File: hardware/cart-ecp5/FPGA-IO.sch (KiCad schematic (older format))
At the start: 9 parts, among them J1 JTAG, U1 LFE5U-25F-xBG256x, U2 W25Q128JVSIM, X1 XO_Generic_NC

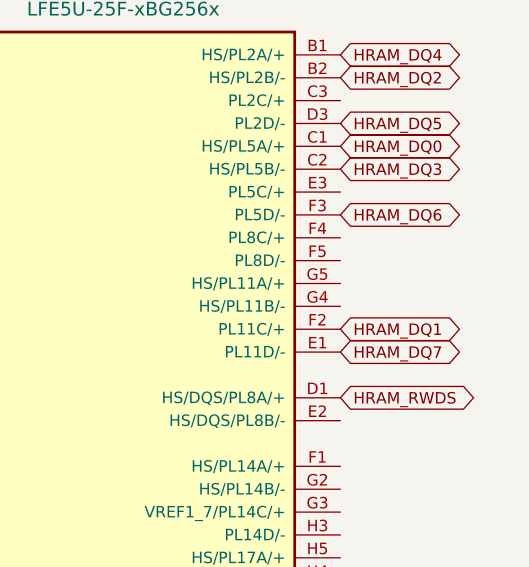
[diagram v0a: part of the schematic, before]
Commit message: First attempt at length tuning hyperram interface
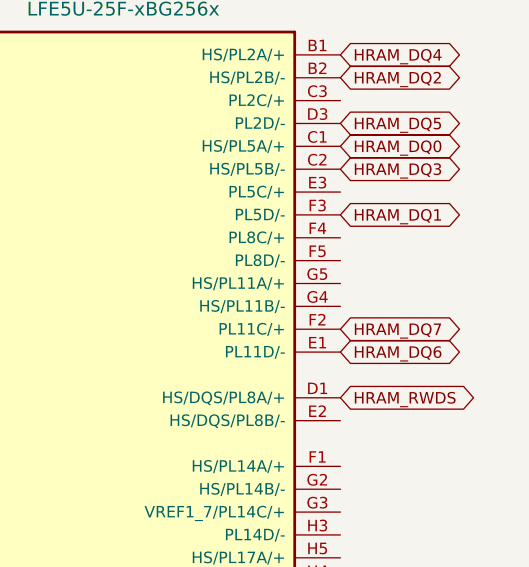
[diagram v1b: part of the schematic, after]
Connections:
- net HRAM_DQ1: now also U1.F3 (PL5D/-); no longer U1.F2 (PL11C/+)
- net HRAM_DQ6: now also U1.E1 (PL11D/-); no longer U1.F3 (PL5D/-)
- net HRAM_DQ7: now also U1.F2 (PL11C/+); no longer U1.E1 (PL11D/-)
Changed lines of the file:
@@
 Text GLabel 13700 6000 2    50   BiDi ~ 0
 HRAM_DQ0
-Text GLabel 13700 6800 2    50   BiDi ~ 0
+Text GLabel 13700 6300 2    50   BiDi ~ 0
 HRAM_DQ1
 Text GLabel 13700 5700 2    50   BiDi ~ 0
@@
 Text GLabel 13700 5900 2    50   BiDi ~ 0
 HRAM_DQ5
-Text GLabel 13700 6300 2    50   BiDi ~ 0
+Text GLabel 13700 6900 2    50   BiDi ~ 0
 HRAM_DQ6
-Text GLabel 13700 6900 2    50   BiDi ~ 0
+Text GLabel 13700 6800 2    50   BiDi ~ 0
 HRAM_DQ7
 Text GLabel 13700 7100 2    50   BiDi ~ 0

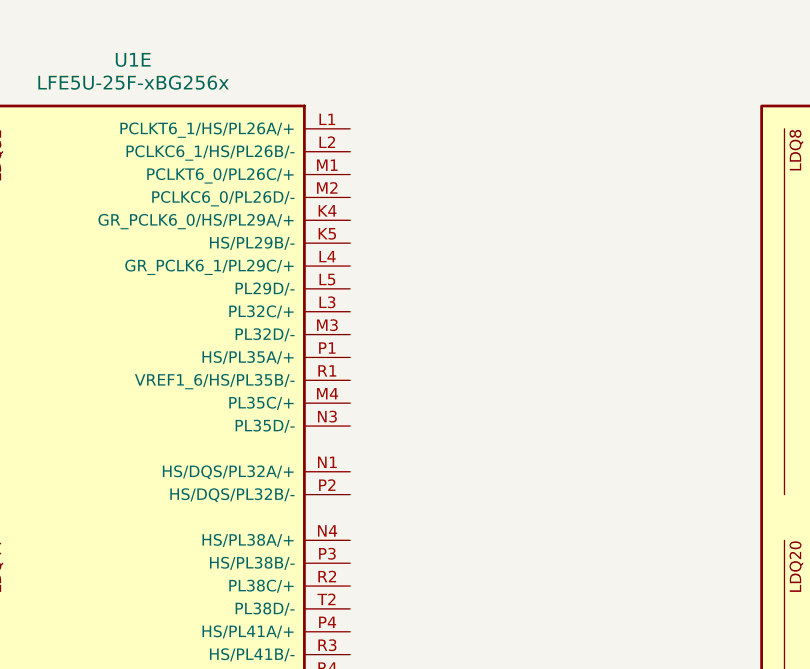
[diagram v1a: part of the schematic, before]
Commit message: Preliminary pin assignment for MicroSD interface
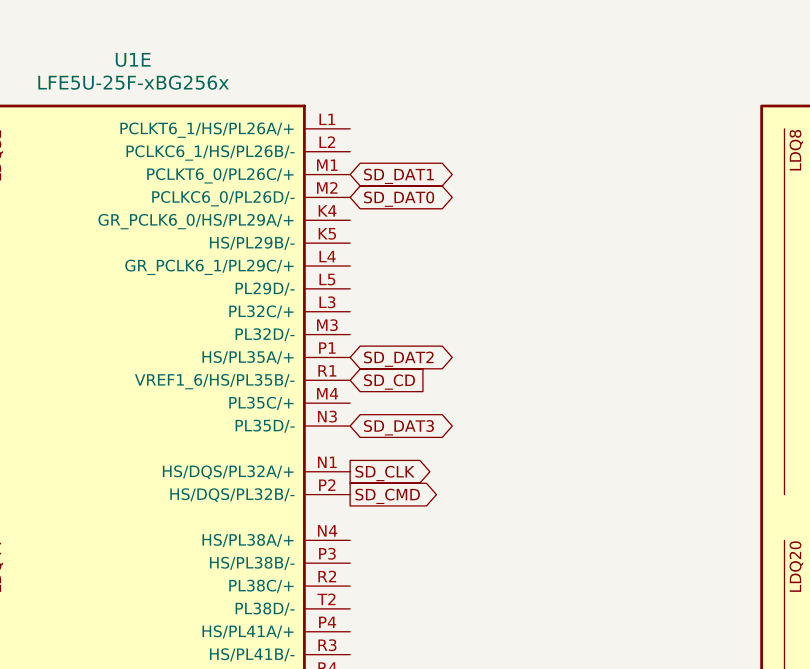
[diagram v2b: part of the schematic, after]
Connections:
- net SD_DAT1: now reaches U1.M1 (PCLKT6_0/PL26C/+)
- net SD_DAT0: now reaches U1.M2 (PCLKC6_0/PL26D/-)
- net SD_CLK: now reaches U1.N1 (HS/DQS/PL32A/+)
- net SD_DAT3: now reaches U1.N3 (PL35D/-)
- net SD_DAT2: now reaches U1.P1 (HS/PL35A/+)
- net SD_CMD: now reaches U1.P2 (HS/DQS/PL32B/-)
- net SD_CD: now reaches U1.R1 (VREF1_6/HS/PL35B/-)
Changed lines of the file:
@@
 Text GLabel 13700 8700 2    50   Output ~ 0
 HRAM_RESET_B
+Text GLabel 10200 7100 2    50   Output ~ 0
+SD_CLK
+Text GLabel 10200 5900 2    50   BiDi ~ 0
+SD_DAT0
+Text GLabel 10200 5800 2    50   BiDi ~ 0
+SD_DAT1
+Text GLabel 10200 7200 2    50   Output ~ 0
+SD_CMD
+Text GLabel 10200 6900 2    50   BiDi ~ 0
+SD_DAT3
+Text GLabel 10200 6600 2    50   BiDi ~ 0
+SD_DAT2
+Text GLabel 10200 6700 2    50   Input ~ 0
+SD_CD
 $EndSCHEMATC

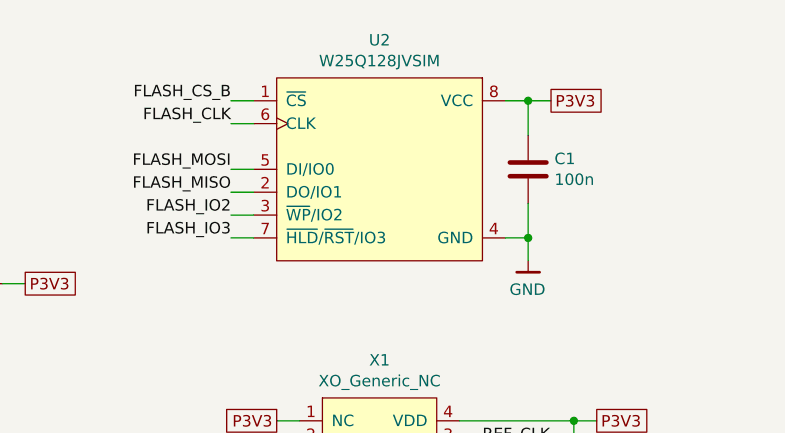
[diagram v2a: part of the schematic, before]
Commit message: Update config flash to WSON package, add HyperRAM decoupling
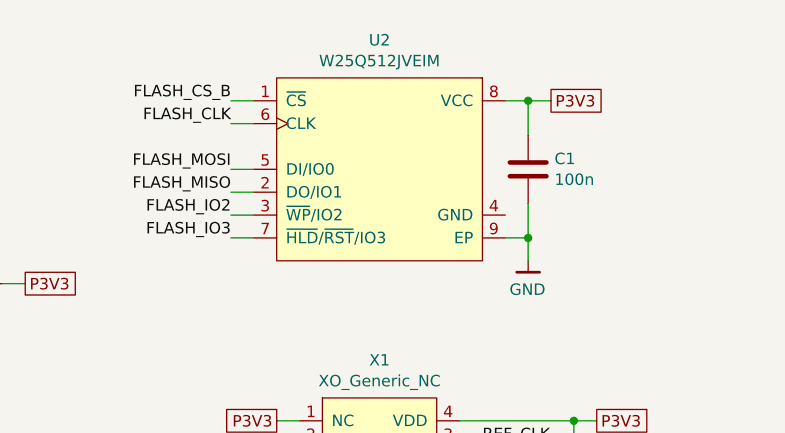
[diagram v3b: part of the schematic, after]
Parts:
- removed U2: W25Q128JVSIM, Package_SO:SOIC-8_5.275x5.275mm_P1.27mm, symbol ng_memory:W25Q128JVSIM
- added U2: W25Q512JVEIM, Package_SON:WSON-8-1EP_6x5mm_P1.27mm_EP3.4x4.3mm, symbol ng_memory:W25Q512JVEIM
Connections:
- net FLASH_CLK: now also U2.6 (CLK)
- net FLASH_CS_B: now also U2.1 (~CS)
- net FLASH_IO2: now also U2.3 (~WP~/IO2)
- net FLASH_IO3: now also U2.7 (~HLD~/~RST~/IO3)
- net FLASH_MISO: now also U2.2 (DO/IO1)
- net FLASH_MOSI: now also U2.5 (DI/IO0)
- net GND: now also U2.9 (EP)
- net P3V3: now also U2.8 (VCC)
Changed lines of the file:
@@
 Comment4 ""
 $EndDescr
-$Comp
-L ng_memory:W25Q128JVSIM U2
-U 1 1 5F3FC315
-P 13200 1500
-F 0 "U2" H 13650 1665 50  0000 C CNN
-F 1 "W25Q128JVSIM" H 13650 1574 50  0000 C CNN
-F 2 "Package_SO:SOIC-8_5.275x5.275mm_P1.27mm" H 13700 650 50  0001 C CNN
-F 3 "https://www.mouser.com/datasheet/2/949/w25q32jv_dtr_revg_03272018_plus-1489786.pdf" H 14200 1200 50  0001 C CNN
-	1    13200 1500
-	-1   0    0    -1
-$EndComp
 Wire Wire Line
 	12200 1600 12100 1600
@@
 Text GLabel 10200 6700 2    50   Input ~ 0
 SD_CD
+$Comp
+L ng_memory:W25Q512JVEIM U2
+U 1 1 5F5A1820
+P 13200 1500
+F 0 "U2" H 13650 1665 50  0000 C CNN
+F 1 "W25Q512JVEIM" H 13650 1574 50  0000 C CNN
+F 2 "Package_SON:WSON-8-1EP_6x5mm_P1.27mm_EP3.4x4.3mm" H 13650 650 50  0001 C CNN
+F 3 "https://www.winbond.com/resource-files/W25Q512JV%20DTR%20RevC%2009102019%20133.pdf" H 14200 1200 50  0001 C CNN
+	1    13200 1500
+	-1   0    0    -1
+$EndComp
 $EndSCHEMATC

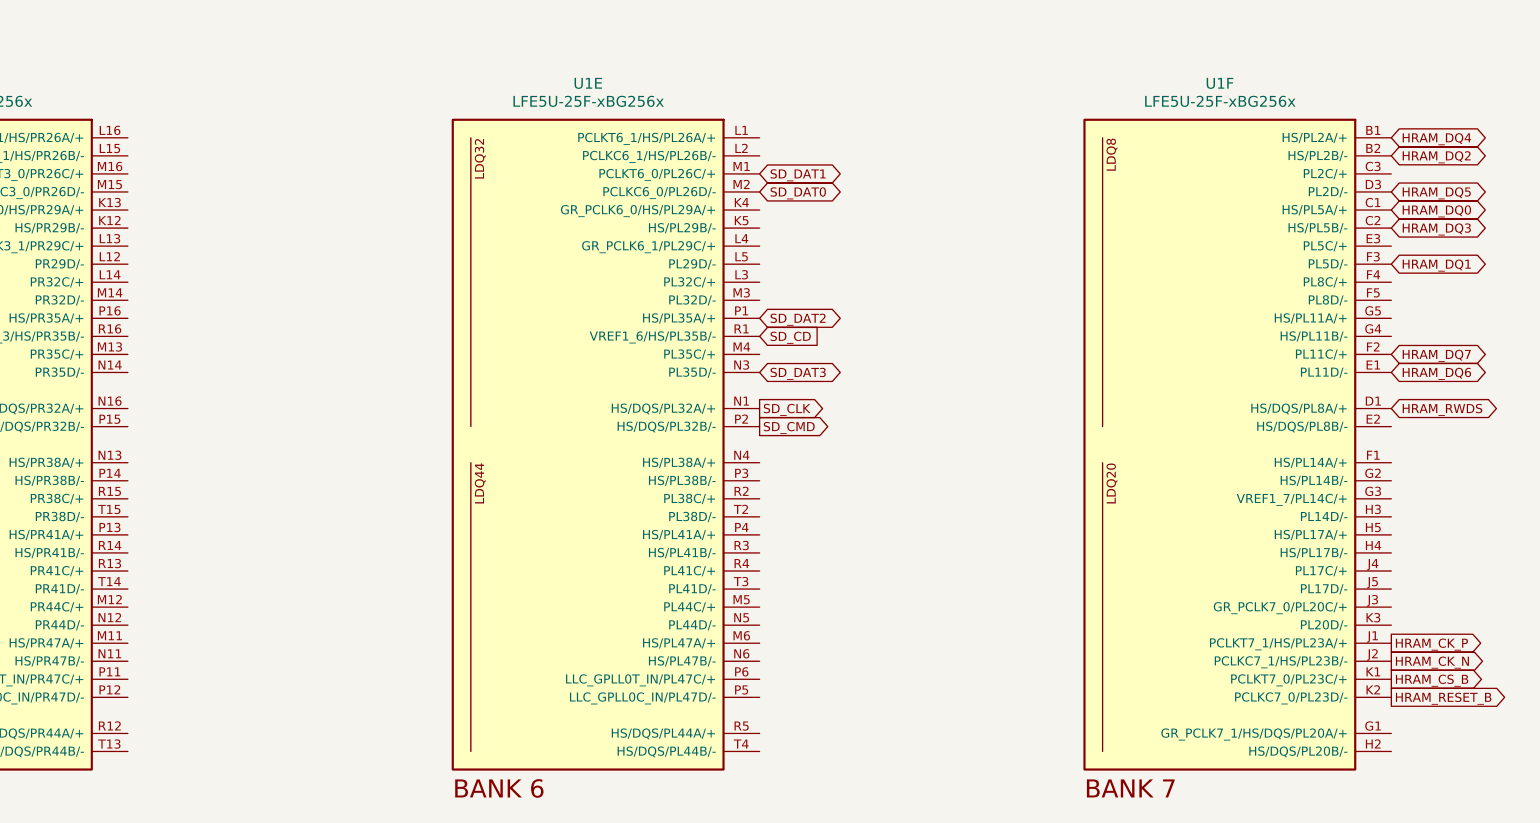
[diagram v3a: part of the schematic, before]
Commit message: Assign FPGA pins to USB interface
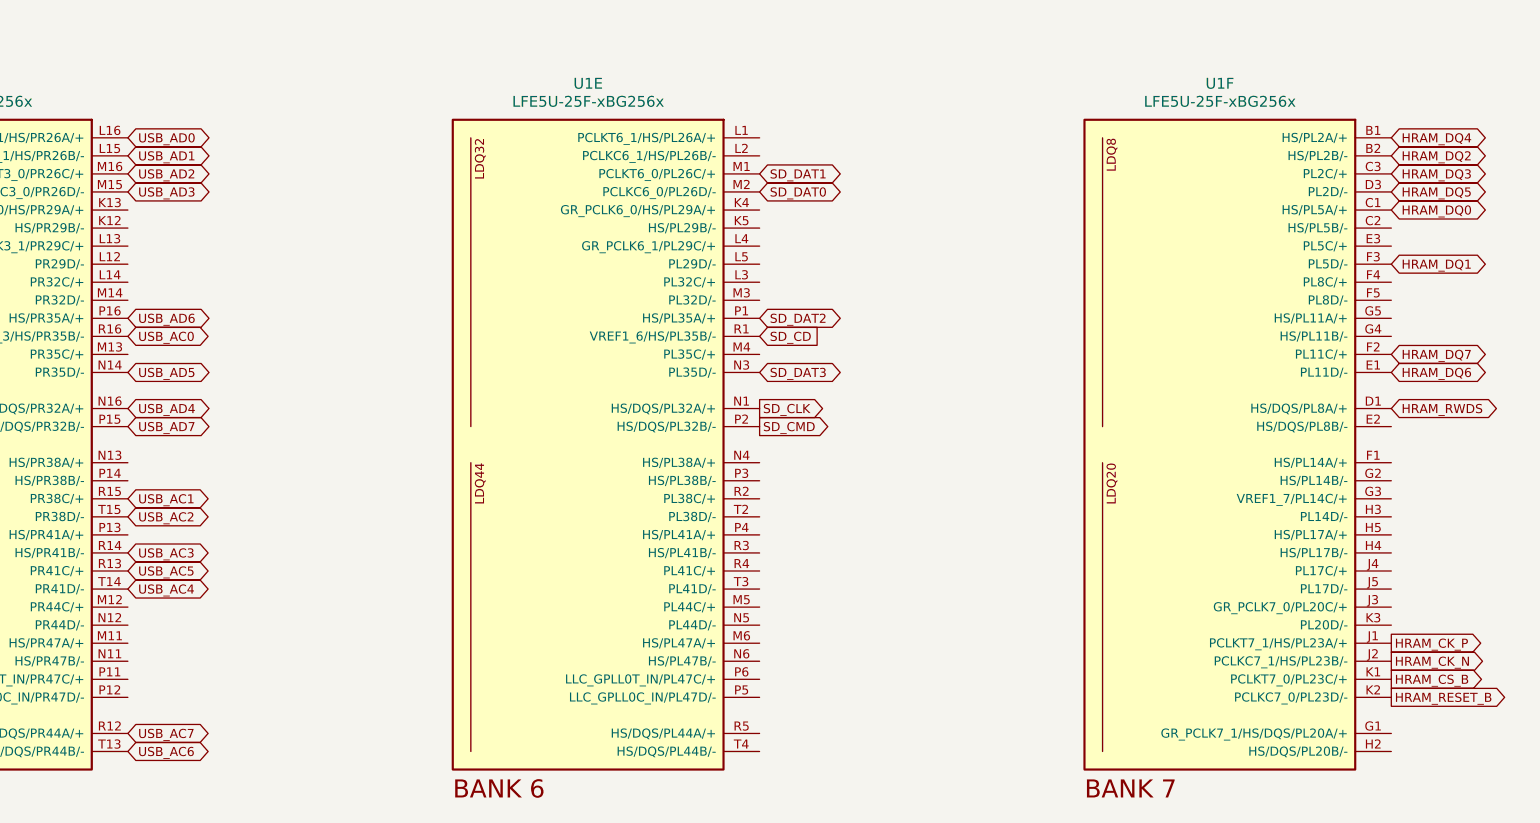
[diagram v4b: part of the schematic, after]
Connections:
- net HRAM_DQ3: now also U1.C3 (PL2C/+); no longer U1.C2 (HS/PL5B/-)
- net USB_AD1: now reaches U1.L15 (PCLKC3_1/HS/PR26B/-)
- net USB_AD0: now reaches U1.L16 (PCLKT3_1/HS/PR26A/+)
- net USB_AD3: now reaches U1.M15 (PCLKC3_0/PR26D/-)
- net USB_AD2: now reaches U1.M16 (PCLKT3_0/PR26C/+)
- net USB_AD5: now reaches U1.N14 (PR35D/-)
- net USB_AD4: now reaches U1.N16 (HS/DQS/PR32A/+)
- net USB_AD7: now reaches U1.P15 (HS/DQS/PR32B/-)
- net USB_AD6: now reaches U1.P16 (HS/PR35A/+)
- net USB_AC7: now reaches U1.R12 (HS/DQS/PR44A/+)
- net USB_AC5: now reaches U1.R13 (PR41C/+)
- net USB_AC3: now reaches U1.R14 (HS/PR41B/-)
- net USB_AC1: now reaches U1.R15 (PR38C/+)
- net USB_AC0: now reaches U1.R16 (VREF1_3/HS/PR35B/-)
- net USB_AC6: now reaches U1.T13 (HS/DQS/PR44B/-)
- net USB_AC4: now reaches U1.T14 (PR41D/-)
- net USB_AC2: now reaches U1.T15 (PR38D/-)
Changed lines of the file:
@@
 Text GLabel 13700 5700 2    50   BiDi ~ 0
 HRAM_DQ2
-Text GLabel 13700 6100 2    50   BiDi ~ 0
+Text GLabel 13700 5800 2    50   BiDi ~ 0
 HRAM_DQ3
 Text GLabel 13700 5600 2    50   BiDi ~ 0
@@
 	-1   0    0    -1
 $EndComp
+Text GLabel 6700 5600 2    50   BiDi ~ 0
+USB_AD0
+Text GLabel 6700 5700 2    50   BiDi ~ 0
+USB_AD1
+Text GLabel 6700 5800 2    50   BiDi ~ 0
+USB_AD2
+Text GLabel 6700 5900 2    50   BiDi ~ 0
+USB_AD3
+Text GLabel 6700 7100 2    50   BiDi ~ 0
+USB_AD4
+Text GLabel 6700 6900 2    50   BiDi ~ 0
+USB_AD5
+Text GLabel 6700 6600 2    50   BiDi ~ 0
+USB_AD6
+Text GLabel 6700 7200 2    50   BiDi ~ 0
+USB_AD7
+Text GLabel 6700 6700 2    50   BiDi ~ 0
+USB_AC0
+Text GLabel 6700 7600 2    50   BiDi ~ 0
+USB_AC1
+Text GLabel 6700 7700 2    50   BiDi ~ 0
+USB_AC2
+Text GLabel 6700 7900 2    50   BiDi ~ 0
+USB_AC3
+Text GLabel 6700 8100 2    50   BiDi ~ 0
+USB_AC4
+Text GLabel 6700 8000 2    50   BiDi ~ 0
+USB_AC5
+Text GLabel 6700 9000 2    50   BiDi ~ 0
+USB_AC6
+Text GLabel 6700 8900 2    50   BiDi ~ 0
+USB_AC7
 $EndSCHEMATC

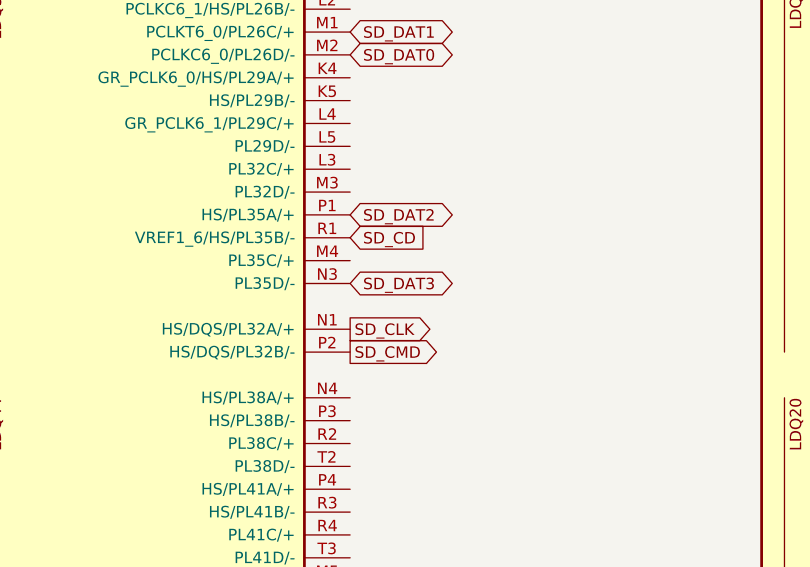
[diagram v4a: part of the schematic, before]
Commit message: Preliminary routing of MicroSD interface
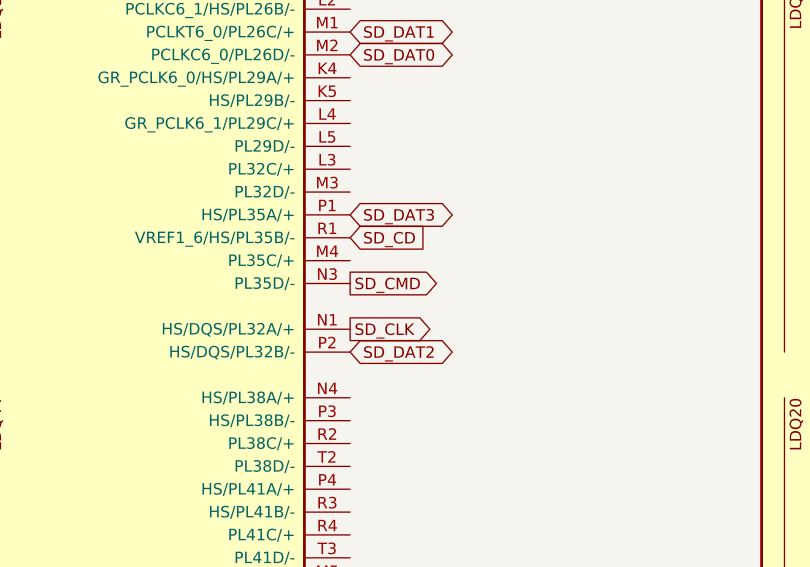
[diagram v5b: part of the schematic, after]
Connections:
- net SD_CMD: now also U1.N3 (PL35D/-); no longer U1.P2 (HS/DQS/PL32B/-)
- net SD_DAT2: now also U1.P2 (HS/DQS/PL32B/-); no longer U1.P1 (HS/PL35A/+)
- net SD_DAT3: now also U1.P1 (HS/PL35A/+); no longer U1.N3 (PL35D/-)
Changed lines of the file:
@@
 Text GLabel 10200 5800 2    50   BiDi ~ 0
 SD_DAT1
-Text GLabel 10200 7200 2    50   Output ~ 0
+Text GLabel 10200 6900 2    50   Output ~ 0
 SD_CMD
-Text GLabel 10200 6900 2    50   BiDi ~ 0
+Text GLabel 10200 6600 2    50   BiDi ~ 0
 SD_DAT3
-Text GLabel 10200 6600 2    50   BiDi ~ 0
+Text GLabel 10200 7200 2    50   BiDi ~ 0
 SD_DAT2
 Text GLabel 10200 6700 2    50   Input ~ 0

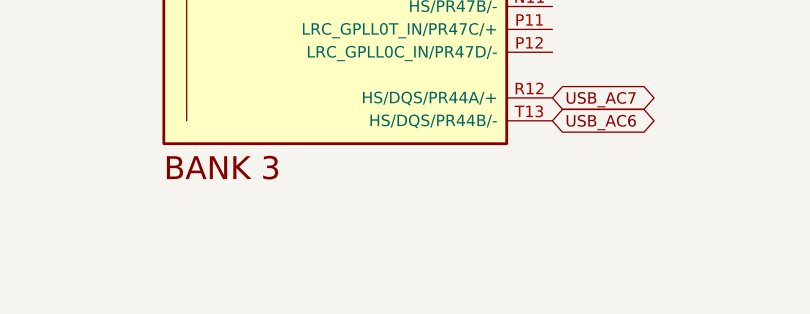
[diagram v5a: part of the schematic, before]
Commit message: Begin to layout USB interface subcircuit
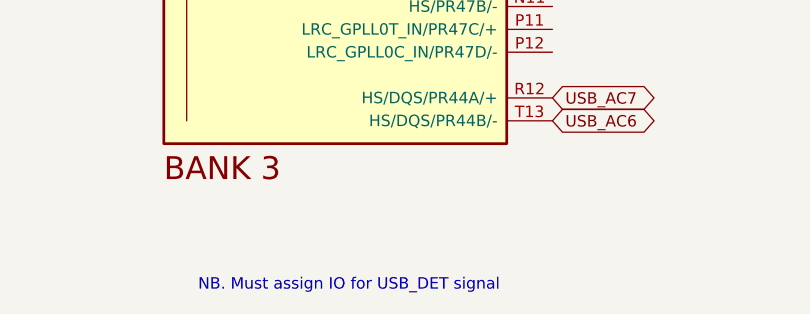
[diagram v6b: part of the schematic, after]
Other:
- note added: "NB. Must assign IO for USB_DET signal"
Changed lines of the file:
@@
 Text GLabel 6700 8900 2    50   BiDi ~ 0
 USB_AC7
+Text Notes 5150 9750 0    50   ~ 0
+NB. Must assign IO for USB_DET signal
 $EndSCHEMATC
